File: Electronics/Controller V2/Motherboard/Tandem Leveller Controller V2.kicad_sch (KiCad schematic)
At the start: 6 parts, among them J8 776180-1, J9 776279-1

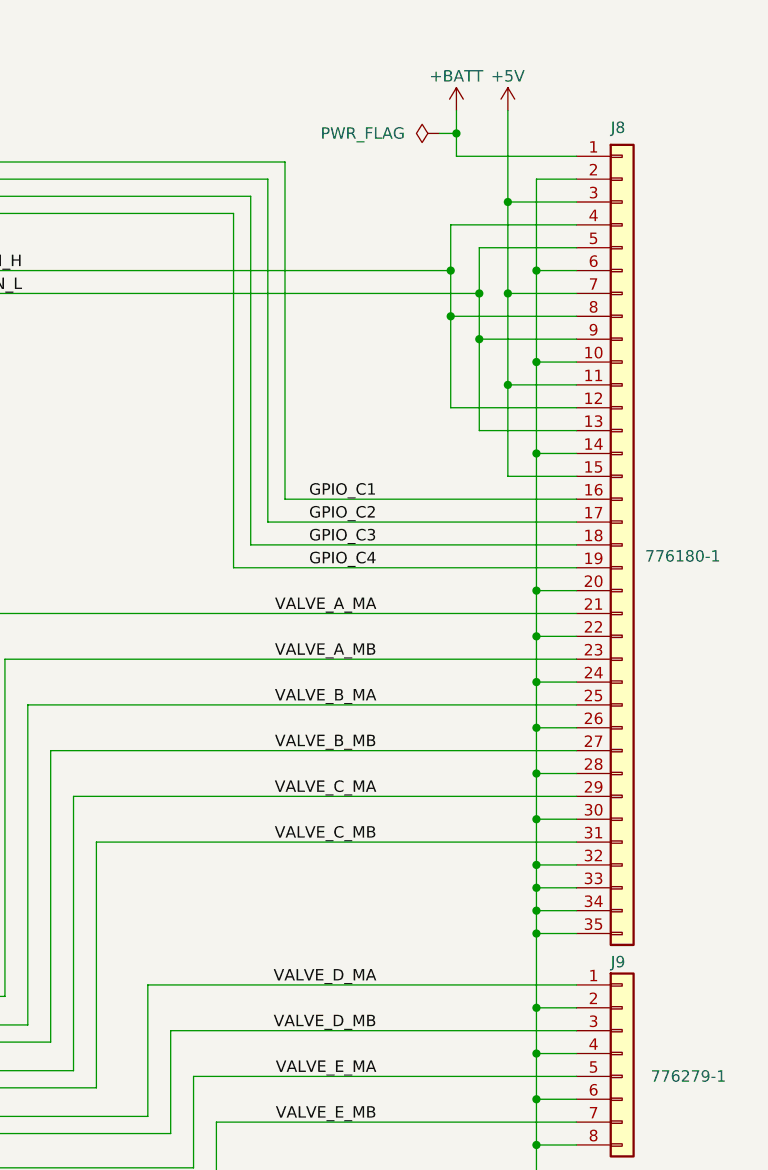
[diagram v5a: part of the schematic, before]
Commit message: Added missing ground connection. Working on PCB layout.
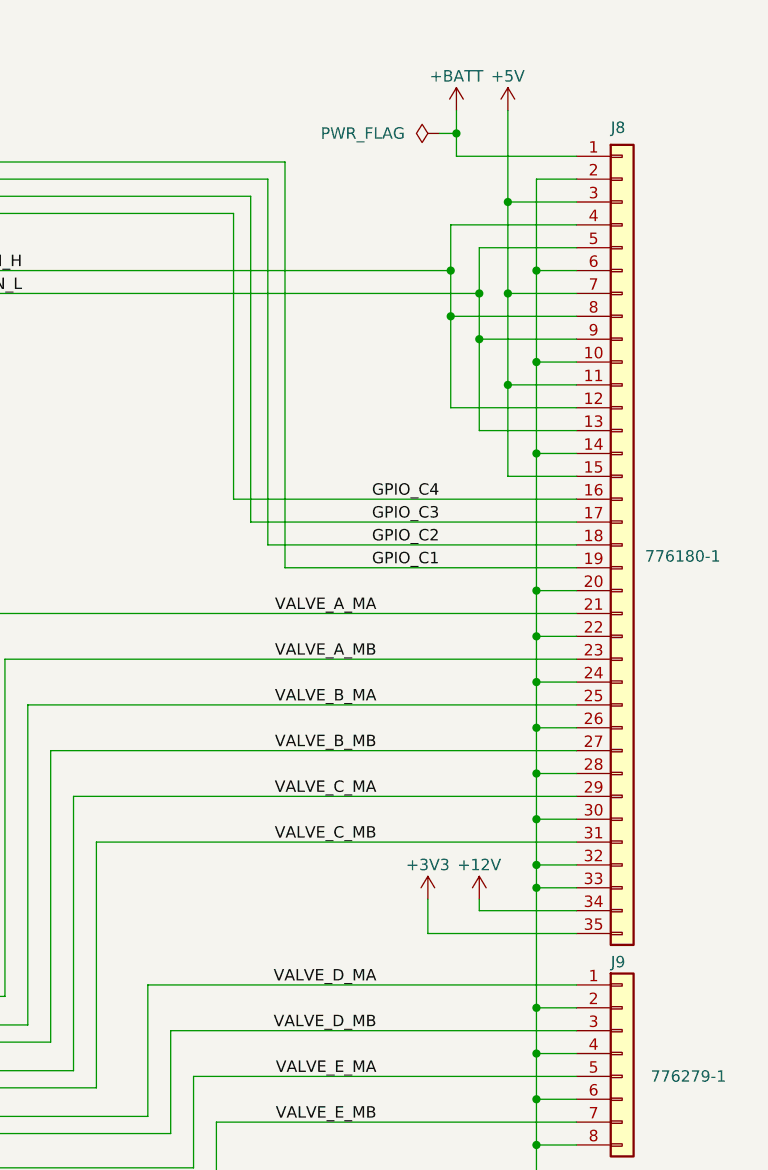
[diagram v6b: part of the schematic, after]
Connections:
- net GND: no longer J8.34 (Pin_34), J8.35 (Pin_35)
- net GPIO_C1: now also J8.19 (Pin_19); no longer J8.16 (Pin_16)
- net GPIO_C2: now also J8.18 (Pin_18); no longer J8.17 (Pin_17)
- net GPIO_C3: now also J8.17 (Pin_17); no longer J8.18 (Pin_18)
- net GPIO_C4: now also J8.16 (Pin_16); no longer J8.19 (Pin_19)
- new net +12V: J8.34 (Pin_34)
- new net +3V3: J8.35 (Pin_35)
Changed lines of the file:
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@@
   (title_block
     (title "Tandem Leveller Controller")
-    (date "2026-02-02")
+    (date "2026-02-06")
     (rev "V2.0")
     (company "(C) andy@britishideas.com 2026")
@@
   (junction (at 227.33 62.865) (diameter 0) (color 0 0 0 0)
   )
-  (junction (at 233.68 128.905) (diameter 0) (color 0 0 0 0)
-  )
   (junction (at 233.68 147.32) (diameter 0) (color 0 0 0 0)
   )
@@
   (junction (at 230.505 47.625) (diameter 0) (color 0 0 0 0)
   )
-  (junction (at 233.68 126.365) (diameter 0) (color 0 0 0 0)
-  )
   (junction (at 224.155 55.245) (diameter 0) (color 0 0 0 0)
   )
@@
     (stroke (width 0) (type default))
   )
-  (wire (pts (xy 203.835 83.185) (xy 238.125 83.185))
-    (stroke (width 0) (type default))
-  )
   (wire (pts (xy 172.085 133.985) (xy 172.085 93.345))
     (stroke (width 0) (type default))
@@
     (stroke (width 0) (type default))
   )
+  (wire (pts (xy 221.615 125.095) (xy 221.615 128.905))
+    (stroke (width 0) (type default))
+  )
   (wire (pts (xy 168.91 140.97) (xy 179.705 140.97))
     (stroke (width 0) (type default))
@@
     (stroke (width 0) (type default))
   )
-  (wire (pts (xy 233.68 126.365) (xy 238.125 126.365))
+  (wire (pts (xy 203.835 85.725) (xy 238.125 85.725))
     (stroke (width 0) (type default))
   )
@@
     (stroke (width 0) (type default))
   )
-  (wire (pts (xy 200.025 48.895) (xy 200.025 88.265))
+  (wire (pts (xy 200.025 48.895) (xy 200.025 80.645))
     (stroke (width 0) (type default))
   )
@@
     (stroke (width 0) (type default))
   )
-  (wire (pts (xy 205.74 80.645) (xy 238.125 80.645))
-    (stroke (width 0) (type default))
-  )
   (wire (pts (xy 230.505 67.945) (xy 230.505 57.785))
     (stroke (width 0) (type default))
@@
     (stroke (width 0) (type default))
   )
-  (wire (pts (xy 233.68 128.905) (xy 238.125 128.905))
-    (stroke (width 0) (type default))
-  )
-  (wire (pts (xy 201.93 85.725) (xy 238.125 85.725))
-    (stroke (width 0) (type default))
-  )
   (wire (pts (xy 132.715 84.455) (xy 136.525 84.455))
     (stroke (width 0) (type default))
@@
     (stroke (width 0) (type default))
   )
+  (wire (pts (xy 200.025 80.645) (xy 238.125 80.645))
+    (stroke (width 0) (type default))
+  )
   (wire (pts (xy 230.505 57.785) (xy 230.505 47.625))
     (stroke (width 0) (type default))
   )
-  (wire (pts (xy 205.74 43.18) (xy 205.74 80.645))
+  (wire (pts (xy 205.74 43.18) (xy 205.74 88.265))
     (stroke (width 0) (type default))
   )
@@
     (stroke (width 0) (type default))
   )
+  (wire (pts (xy 221.615 128.905) (xy 238.125 128.905))
+    (stroke (width 0) (type default))
+  )
   (wire (pts (xy 233.68 106.045) (xy 238.125 106.045))
     (stroke (width 0) (type default))
@@
     (stroke (width 0) (type default))
   )
+  (wire (pts (xy 227.33 126.365) (xy 238.125 126.365))
+    (stroke (width 0) (type default))
+  )
   (wire (pts (xy 233.68 111.125) (xy 233.68 116.205))
     (stroke (width 0) (type default))
@@
     (stroke (width 0) (type default))
   )
-  (wire (pts (xy 200.025 88.265) (xy 238.125 88.265))
-    (stroke (width 0) (type default))
-  )
   (wire (pts (xy 132.715 121.285) (xy 136.525 121.285))
     (stroke (width 0) (type default))
@@
     (stroke (width 0) (type default))
   )
-  (wire (pts (xy 233.68 137.16) (xy 233.68 128.905))
+  (wire (pts (xy 233.68 123.825) (xy 233.68 137.16))
     (stroke (width 0) (type default))
   )
@@
     (stroke (width 0) (type default))
   )
-  (wire (pts (xy 203.835 45.085) (xy 203.835 83.185))
+  (wire (pts (xy 203.835 45.085) (xy 203.835 85.725))
     (stroke (width 0) (type default))
   )
@@
     (stroke (width 0) (type default))
   )
+  (wire (pts (xy 201.93 83.185) (xy 238.125 83.185))
+    (stroke (width 0) (type default))
+  )
   (wire (pts (xy 195.58 144.78) (xy 238.125 144.78))
     (stroke (width 0) (type default))
   )
-  (wire (pts (xy 233.68 126.365) (xy 233.68 123.825))
-    (stroke (width 0) (type default))
-  )
   (wire (pts (xy 224.155 70.485) (xy 224.155 60.325))
     (stroke (width 0) (type default))
@@
     (stroke (width 0) (type default))
   )
-  (wire (pts (xy 201.93 46.99) (xy 201.93 85.725))
+  (wire (pts (xy 201.93 46.99) (xy 201.93 83.185))
     (stroke (width 0) (type default))
   )
@@
     (stroke (width 0) (type default))
   )
-  (wire (pts (xy 233.68 128.905) (xy 233.68 126.365))
-    (stroke (width 0) (type default))
-  )
   (wire (pts (xy 224.79 37.465) (xy 224.79 40.005))
     (stroke (width 0) (type default))
@@
     (stroke (width 0) (type default))
   )
+  (wire (pts (xy 227.33 125.095) (xy 227.33 126.365))
+    (stroke (width 0) (type default))
+  )
   (wire (pts (xy 168.91 151.13) (xy 193.04 151.13))
     (stroke (width 0) (type default))
@@
     (stroke (width 0) (type default))
   )
+  (wire (pts (xy 205.74 88.265) (xy 238.125 88.265))
+    (stroke (width 0) (type default))
+  )
   (wire (pts (xy 177.165 139.065) (xy 177.165 103.505))
     (stroke (width 0) (type default))
@@
     (effects (font (size 1.27 1.27)) (justify right bottom))
   )
-  (label "GPIO_C1" (at 215.9 80.645 180) (fields_autoplaced)
+  (label "GPIO_C1" (at 222.885 88.265 180) (fields_autoplaced)
     (effects (font (size 1.27 1.27)) (justify right bottom))
   )
@@
     (effects (font (size 1.27 1.27)) (justify right bottom))
   )
-  (label "GPIO_C4" (at 215.9 88.265 180) (fields_autoplaced)
+  (label "GPIO_C4" (at 222.885 80.645 180) (fields_autoplaced)
     (effects (font (size 1.27 1.27)) (justify right bottom))
   )
@@
     (effects (font (size 1.27 1.27)) (justify right bottom))
   )
-  (label "GPIO_C2" (at 215.9 83.185 180) (fields_autoplaced)
-    (effects (font (size 1.27 1.27)) (justify right bottom))
-  )
-  (label "GPIO_C3" (at 215.9 85.725 180) (fields_autoplaced)
+  (label "GPIO_C2" (at 222.885 85.725 180) (fields_autoplaced)
+    (effects (font (size 1.27 1.27)) (justify right bottom))
+  )
+  (label "GPIO_C3" (at 222.885 83.185 180) (fields_autoplaced)
     (effects (font (size 1.27 1.27)) (justify right bottom))
   )
@@
   (label "VALVE_D_MA" (at 215.9 134.62 180) (fields_autoplaced)
     (effects (font (size 1.27 1.27)) (justify right bottom))
+  )
+  (symbol (lib_id "power:+12V") (at 227.33 125.095 0) (unit 1)
+    (in_bom yes) (on_board yes) (dnp no)
+    (property "Reference" "#PWR038" (at 227.33 128.905 0)
+      (effects (font (size 1.27 1.27)) hide)
+    )
+    (property "Value" "+12V" (at 227.33 121.285 0)
+      (effects (font (size 1.27 1.27)))
+    )
+    (property "Footprint" "" (at 227.33 125.095 0)
+      (effects (font (size 1.27 1.27)) hide)
+    )
+    (property "Datasheet" "" (at 227.33 125.095 0)
+      (effects (font (size 1.27 1.27)) hide)
+    )
+    (pin "1")
+    (instances
+      (project "Tandem Leveller Controller V2"
+        (path "/dceffac9-8f5b-4889-8265-b6c471cb5dde"
+          (reference "#PWR038") (unit 1)
+        )
+      )
+    )
   )
   (symbol (lib_id "Mechanical:MountingHole") (at 127 175.895 0) (unit 1)
@@
         )
       )
+    )
+  )
+  (symbol (lib_id "power:+3V3") (at 221.615 125.095 0) (unit 1)
+    (in_bom yes) (on_board yes) (dnp no)
+    (property "Reference" "#PWR036" (at 221.615 128.905 0)
+      (effects (font (size 1.27 1.27)) hide)
+    )
+    (property "Value" "+3V3" (at 221.615 121.285 0)
+      (effects (font (size 1.27 1.27)))
+    )
+    (property "Footprint" "" (at 221.615 125.095 0)
+      (effects (font (size 1.27 1.27)) hide)
+    )
+    (property "Datasheet" "" (at 221.615 125.095 0)
+      (effects (font (size 1.27 1.27)) hide)
+    )
+    (pin "1")
+    (instances
+      (project "Tandem Leveller Controller V2"
+        (path "/dceffac9-8f5b-4889-8265-b6c471cb5dde"
+          (reference "#PWR036") (unit 1)
+        )
+      )

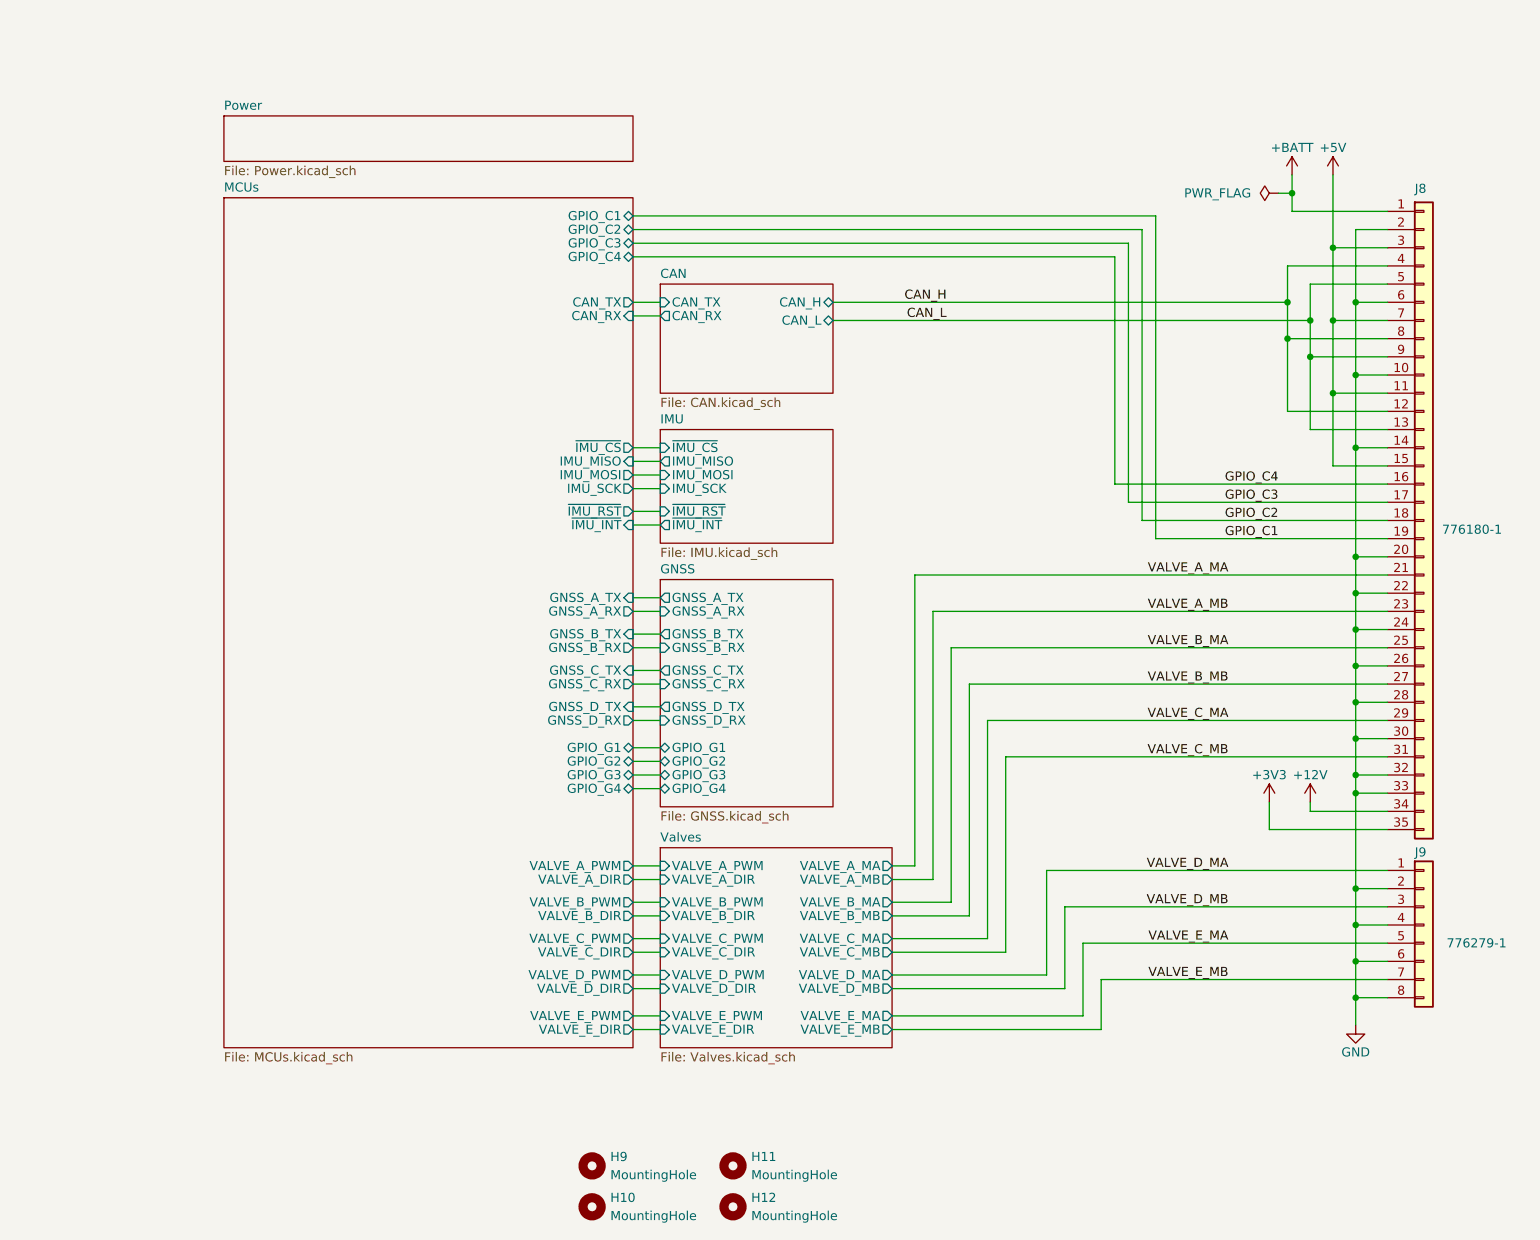
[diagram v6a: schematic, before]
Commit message: Added generic IMU option.
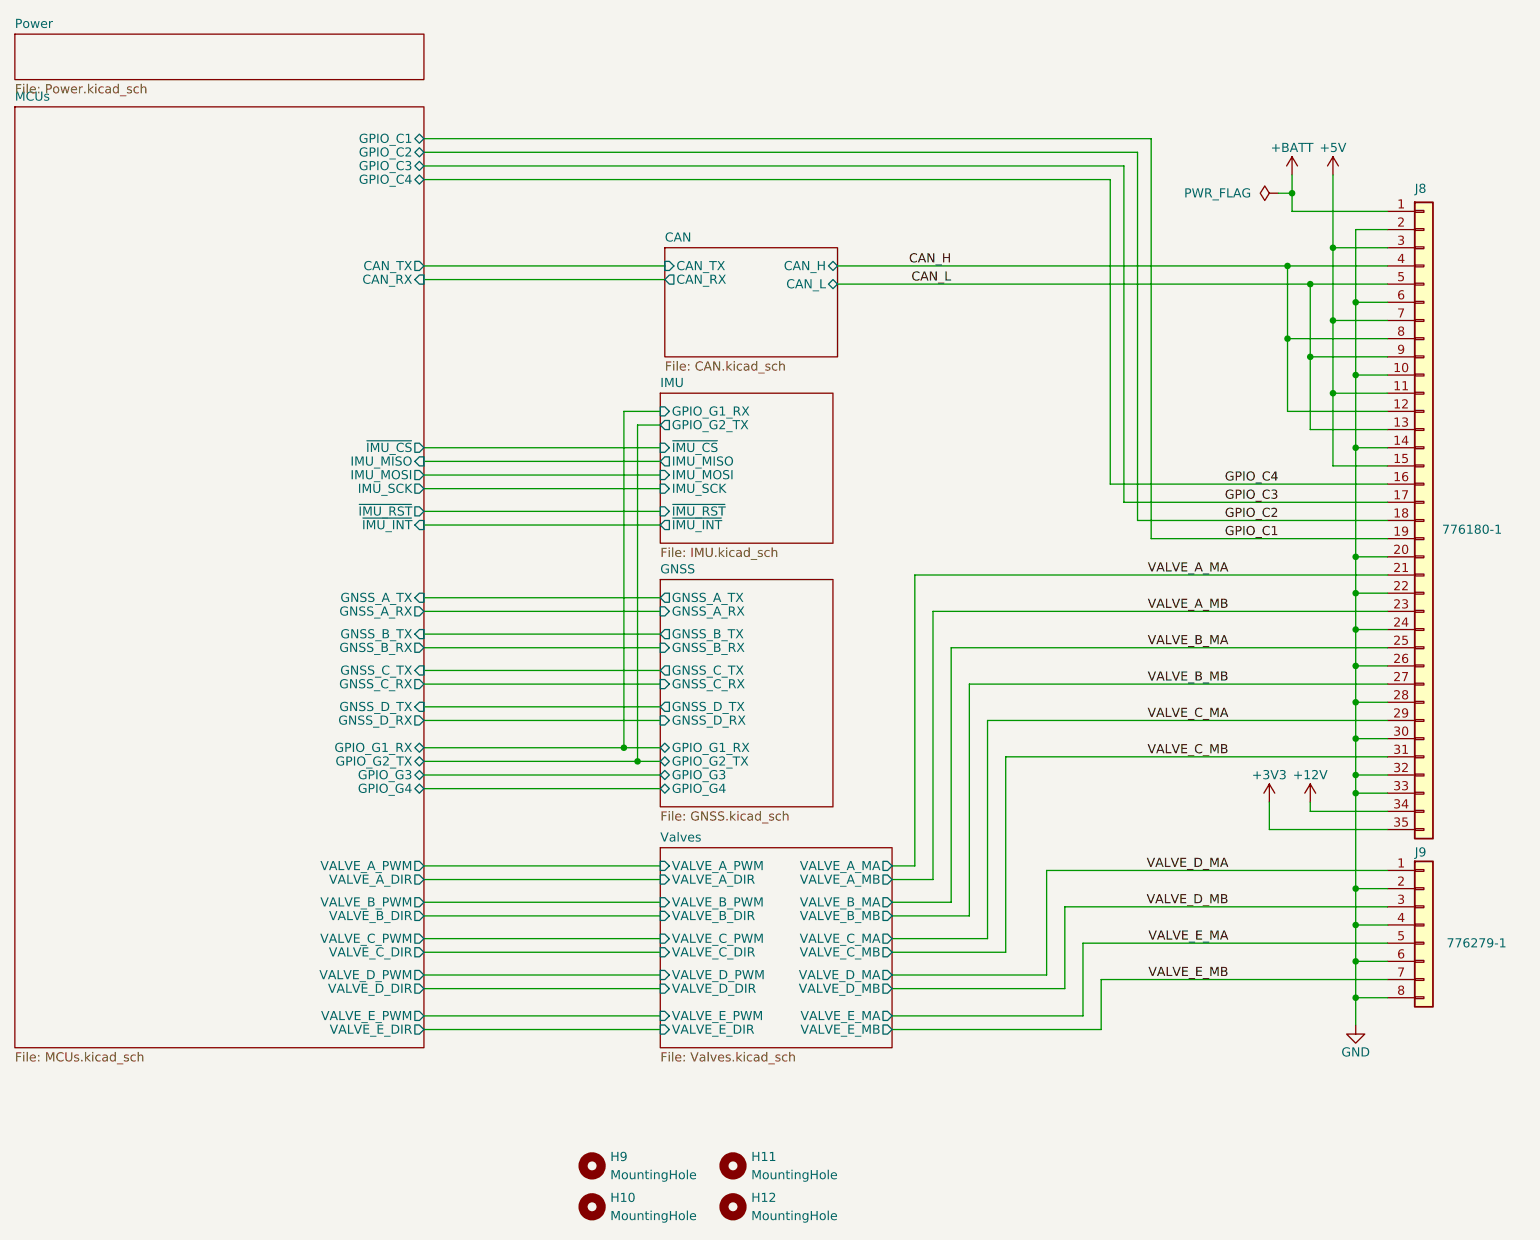
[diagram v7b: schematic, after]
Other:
- sheet GNSS ports: added GPIO_G1_RX, GPIO_G2_TX; removed GPIO_G1, GPIO_G2
- sheet IMU ports: added GPIO_G1_RX, GPIO_G2_TX; removed none
- sheet MCUs ports: added GPIO_G1_RX, GPIO_G2_TX; removed GPIO_G1, GPIO_G2

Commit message: Working on V2 controller board. Started firmware to do list.
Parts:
- H10, H11, H12, H9: footprint MountingHole:MountingHole_3.2mm_M3 -> MountingHole:MountingHole_4mm
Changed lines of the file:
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@@
       (effects (font (size 1.27 1.27)) (justify left))
     )
-    (property "Footprint" "MountingHole:MountingHole_3.2mm_M3" (at 127 175.895 0)
+    (property "Footprint" "MountingHole:MountingHole_4mm" (at 127 175.895 0)
       (effects (font (size 1.27 1.27)) hide)
     )
@@
       (effects (font (size 1.27 1.27)) (justify left))
     )
-    (property "Footprint" "MountingHole:MountingHole_3.2mm_M3" (at 127 181.61 0)
+    (property "Footprint" "MountingHole:MountingHole_4mm" (at 127 181.61 0)
       (effects (font (size 1.27 1.27)) hide)
     )
@@
       (effects (font (size 1.27 1.27)) (justify left))
     )
-    (property "Footprint" "MountingHole:MountingHole_3.2mm_M3" (at 146.685 181.61 0)
+    (property "Footprint" "MountingHole:MountingHole_4mm" (at 146.685 181.61 0)
       (effects (font (size 1.27 1.27)) hide)
     )
@@
       (effects (font (size 1.27 1.27)) (justify left))
     )
-    (property "Footprint" "MountingHole:MountingHole_3.2mm_M3" (at 146.685 175.895 0)
-      (effects (font (size 1.27 1.27)) hide)
-    )
+    (property "Footprint" "MountingHole:MountingHole_4mm" (at 146.685 175.895 0)
+      (effects (font (size 1.27 1.27)) hide)
+    )
